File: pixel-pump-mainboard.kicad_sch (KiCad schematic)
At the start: 121 parts, among them J1 JST NC Valve, J10 BM10B-SRSS-TB(LF)(SN), J11 UART/SWD DNP, J12 TYPE-C-31-M-12, J2 JST NO Valve, J3 6P4C, J4 JST 3 Way Valve, J5 Jack-DC 12V, J6 Power Sw, J7 EXP1, J8 EXP2, J9 BM04B-SRSS-TBT(LF)(SN), Q1 BSS138, Q2 BSS138, Q3 BSS138, Q4 STN4NF20L, Q5 BSS138, SW1 BOOTSEL, U1 LD1117S33TR, U2 TPS62112RSAR, U3 W25Q128JVS, U4 RP2040, Y1 445C25D12M00000

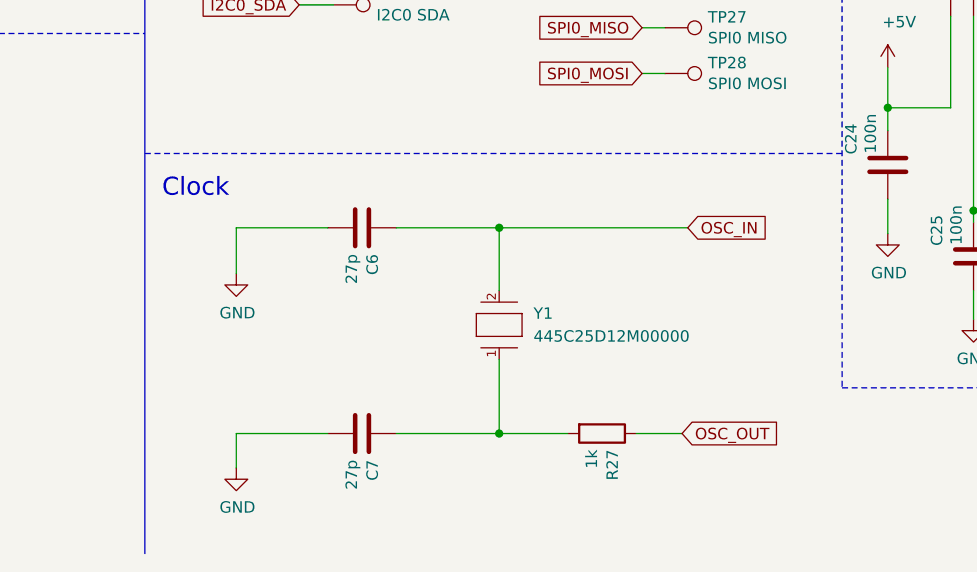
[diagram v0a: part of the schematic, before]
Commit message: Revert back to ABM12 footprint
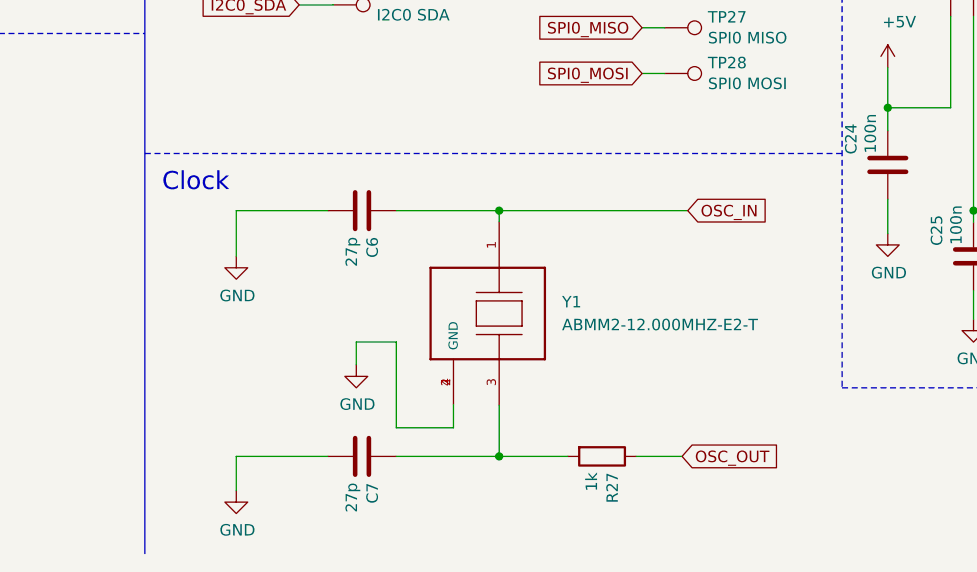
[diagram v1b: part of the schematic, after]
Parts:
- removed Y1: 445C25D12M00000, CTS 445C25D12M00000 12MHz:CTS-445-0-0-0, symbol CTS 445C25D12M00000 12MHz:445C25D12M00000
- added Y1: ABMM2-12.000MHZ-E2-T, ABMM2-12:XTAL_ABMM2-12.000MHZ-E2-T, symbol ABMM2-12.000MHZ-E2-T:ABMM2-12.000MHZ-E2-T
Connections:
- net GND: now also Y1.2 (GND), Y1.4 (GND)
- net OSC_IN: now also Y1.1
- net at C7.1, R27.2: now also Y1.3
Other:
- company: (none) -> Robins Tools
- moved on the sheet: C6, C7, R27

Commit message: Assign all MPNs
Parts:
- C1, C5: MPN (none) -> C3225X5R1E106K250AA
- C10, C12, C13, C16, C17, C18, C19, C20, C22, C23: MPN (none) -> 100n 0402
- C11: MPN (none) -> 10u 0603
- C14, C15: MPN (none) -> 2.2u 0402
- C2: MPN (none) -> 1u 0805
- C21: MPN (none) -> 1n 0603
- C24, C25, C26, C27, C3, C8: MPN (none) -> 100n 0603
- C28, C9, J11: MPN (none) -> DNP
- C4: value 22u 10V -> 22u 16V; MPN (none) -> C3225X7R1C226M250AC
- C6, C7: MPN (none) -> 27p 0603
- D1, D4, D6: MPN (none) -> SP0502BAHT
- D10, D3, D9: MPN (none) -> SOD4007
- D2, D7, D8: MPN (none) -> ORH-G36G DNP
- D5: MPN (none) -> SMAJ12CA
- F1: MPN (none) -> 1812L075PR
- J10: MPN (none) -> BM10B-SRSS-TB(LF)(SN)
- J12: MPN (none) -> TYPE-C-31-M-12
- J3: MPN (none) -> DS1133-S40BPX
- J5: MPN (none) -> 694106301002
- J6: MPN (none) -> WJ500V-5.08-2P; Source https://lcsc.com/product-detail/Pluggable-System-Terminal-B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 -> https://www.lcsc.com/product-detail/Screw-terminal_Ningbo-K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
- J7: MPN (none) -> BM04B-SRSS-TB(LF)(SN)
- J8: MPN (none) -> BM06B-SRSS-TB(LF)(SN)
- J9: MPN (none) -> BM04B-SRSS-TBT(LF)(SN)
- L1, L2: MPN (none) -> SLF7032T-6R8M1R6-2-PF
- Q1, Q2, Q3, Q5: MPN (none) -> BSS138
- Q4: MPN (none) -> STN4NF20L
- R1: MPN (none) -> 5.1k 0402
- R10, R12, R8: MPN (none) -> 68k 0603 DNP
- R11, R6, R9: MPN (none) -> 100k 0603
- R13: MPN (none) -> 100 0603
- R14, R3: MPN (none) -> 1M 0603
- R15, R17, R23, R24, R7: MPN (none) -> 220 0603
- R19: MPN (none) -> 0 0805 DNP
- R2: MPN (none) -> 5.1k 0603
- R20, R25, R29: MPN (none) -> 10k 0603
- R21, R22: MPN (none) -> 2.2k 0603
- R26, R27: MPN (none) -> 1k 0603
- R28: MPN (none) -> 10k 0603 DNP
- R4, R5: MPN (none) -> 27.4 0402
- SW1: MPN (none) -> 1825027-5
- U1: MPN (none) -> LD1117S33TR
- U3: value W25Q128JVS -> W25Q128JVPIQ; MPN (none) -> W25Q128JVPIQ
- U4: MPN (none) -> RP2040
- Y1: MPN (none) -> ABMM2-12.000MHZ-E2-T

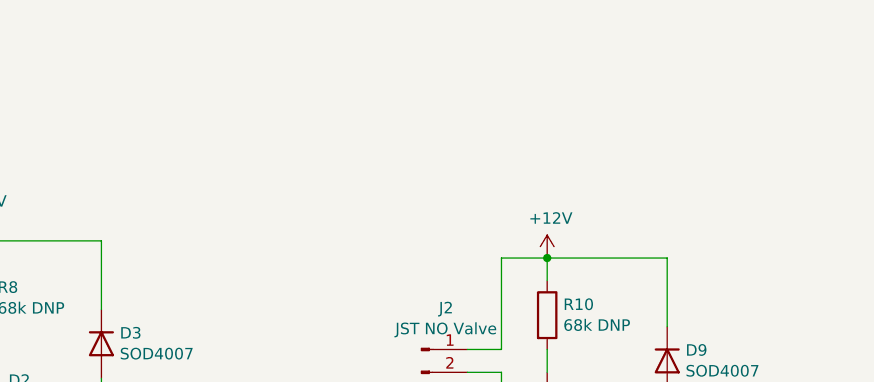
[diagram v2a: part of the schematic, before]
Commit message: Add fiducials and fix THT parts to be SMD
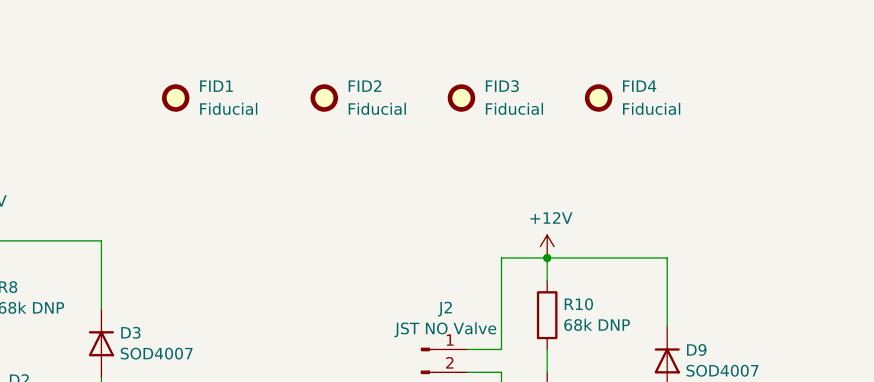
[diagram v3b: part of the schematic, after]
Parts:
- added FID1, FID2, FID3, FID4: Fiducial, Fiducial:Fiducial_0.5mm_Mask1mm, symbol Mechanical:Fiducial
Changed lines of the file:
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@@
+    )
+  )
+  (symbol (lib_id "Mechanical:Fiducial") (at 111.76 21.59 0) (unit 1)
+    (in_bom yes) (on_board yes) (fields_autoplaced)
+    (property "Reference" "FID3" (id 0) (at 114.3 20.3199 0)
+      (effects (font (size 1.27 1.27)) (justify left))
+    )
+    (property "Value" "Fiducial" (id 1) (at 114.3 22.8599 0)
+      (effects (font (size 1.27 1.27)) (justify left))
+    )
+    (property "Footprint" "Fiducial:Fiducial_0.5mm_Mask1mm" (id 2) (at 111.76 21.59 0)
+      (effects (font (size 1.27 1.27)) hide)
+    )
+    (property "Datasheet" "~" (id 3) (at 111.76 21.59 0)
+      (effects (font (size 1.27 1.27)) hide)
     )
   )
@@
     )
     (pin "1")
+  )
+  (symbol (lib_id "Mechanical:Fiducial") (at 80.01 21.59 0) (unit 1)
+    (in_bom yes) (on_board yes) (fields_autoplaced)
+    (property "Reference" "FID1" (id 0) (at 82.55 20.3199 0)
+      (effects (font (size 1.27 1.27)) (justify left))
+    )
+    (property "Value" "Fiducial" (id 1) (at 82.55 22.8599 0)
+      (effects (font (size 1.27 1.27)) (justify left))
+    )
+    (property "Footprint" "Fiducial:Fiducial_0.5mm_Mask1mm" (id 2) (at 80.01 21.59 0)
+      (effects (font (size 1.27 1.27)) hide)
+    )
+    (property "Datasheet" "~" (id 3) (at 80.01 21.59 0)
+      (effects (font (size 1.27 1.27)) hide)
+    )
   )
   (symbol (lib_id "Device:C") (at 199.39 132.08 0) (unit 1)
@@
     (pin "1")
   )
+  (symbol (lib_id "Mechanical:Fiducial") (at 127 21.59 0) (unit 1)
+    (in_bom yes) (on_board yes) (fields_autoplaced)
+    (property "Reference" "FID4" (id 0) (at 129.54 20.3199 0)
+      (effects (font (size 1.27 1.27)) (justify left))
+    )
+    (property "Value" "Fiducial" (id 1) (at 129.54 22.8599 0)
+      (effects (font (size 1.27 1.27)) (justify left))
+    )
+    (property "Footprint" "Fiducial:Fiducial_0.5mm_Mask1mm" (id 2) (at 127 21.59 0)
+      (effects (font (size 1.27 1.27)) hide)
+    )
+    (property "Datasheet" "~" (id 3) (at 127 21.59 0)
+      (effects (font (size 1.27 1.27)) hide)
+    )
+  )
   (symbol (lib_id "TYPE-C-31-M-12:TYPE-C-31-M-12") (at 57.15 235.585 0) (unit 1)
     (in_bom yes) (on_board yes)
@@
     )
   )
+  (symbol (lib_id "Mechanical:Fiducial") (at 96.52 21.59 0) (unit 1)
+    (in_bom yes) (on_board yes) (fields_autoplaced)
+    (property "Reference" "FID2" (id 0) (at 99.06 20.3199 0)
+      (effects (font (size 1.27 1.27)) (justify left))
+    )
+    (property "Value" "Fiducial" (id 1) (at 99.06 22.8599 0)
+      (effects (font (size 1.27 1.27)) (justify left))
+    )
+    (property "Footprint" "Fiducial:Fiducial_0.5mm_Mask1mm" (id 2) (at 96.52 21.59 0)
+      (effects (font (size 1.27 1.27)) hide)
+    )
+    (property "Datasheet" "~" (id 3) (at 96.52 21.59 0)
+      (effects (font (size 1.27 1.27)) hide)
+    )
+  )
   (sheet_instances
     (path "/" (page "1"))
@@
       (reference "F1") (unit 1) (value "1812L075PR") (footprint "Fuse:Fuse_1812_4532Metric")
     )
+    (path "/525bcaf8-d6f5-4066-bfb1-6ce2476103cc"
+      (reference "FID1") (unit 1) (value "Fiducial") (footprint "Fiducial:Fiducial_0.5mm_Mask1mm")
+    )
+    (path "/ff9e6f2a-ecb8-41c5-8eb1-61a3a0969262"
+      (reference "FID2") (unit 1) (value "Fiducial") (footprint "Fiducial:Fiducial_0.5mm_Mask1mm")
+    )
+    (path "/1b6bfdd4-98c5-406d-bac2-cc06853dcd37"
+      (reference "FID3") (unit 1) (value "Fiducial") (footprint "Fiducial:Fiducial_0.5mm_Mask1mm")
+    )
+    (path "/f50fdb03-4e54-439a-b508-d878f9afad01"
+      (reference "FID4") (unit 1) (value "Fiducial") (footprint "Fiducial:Fiducial_0.5mm_Mask1mm")
+    )
     (path "/3d163751-7871-486d-a542-8b4f1d680a2a"

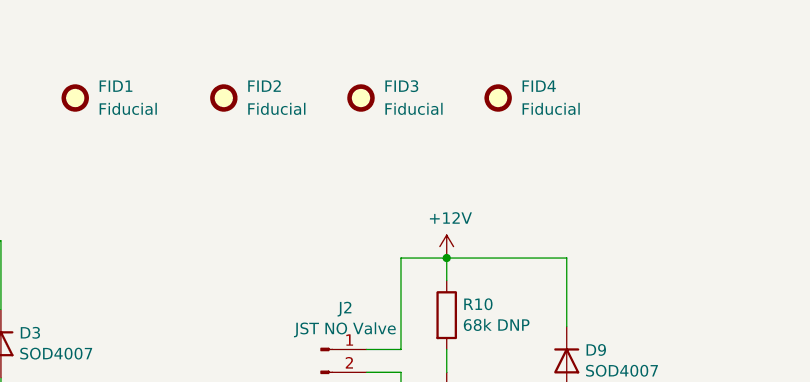
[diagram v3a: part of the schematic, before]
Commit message: Remove DNP parts from BOM, increase Fiducial to 0.75/1.5mm
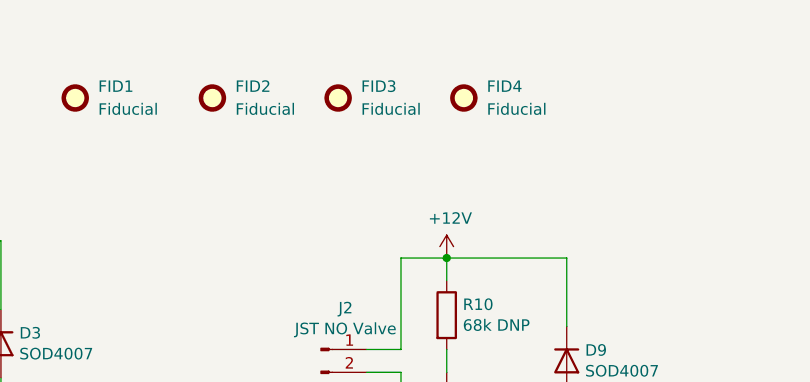
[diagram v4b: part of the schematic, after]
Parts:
- D2, R8: now left out of the parts list
- FID1, FID2, FID3, FID4: footprint Fiducial:Fiducial_0.5mm_Mask1mm -> Fiducial:Fiducial_0.75mm_Mask1.5mm
- J1, J2, J4: MPN (none) -> B2B-XH-A-GU
- Q1, Q2, Q3: MPN BSS138 -> BSS138P
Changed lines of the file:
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@@
       (effects (font (size 1.27 1.27)) (justify left) hide)
     )
-    (property "MPN" "BSS138" (id 4) (at 55.88 67.945 0)
+    (property "MPN" "BSS138P" (id 4) (at 55.88 67.945 0)
       (effects (font (size 1.27 1.27)) hide)
     )
@@
   )
   (symbol (lib_id "Device:R") (at 58.42 43.815 0) (unit 1)
-    (in_bom yes) (on_board yes)
+    (in_bom no) (on_board yes)
     (property "Reference" "R8" (id 0) (at 60.198 42.6466 0)
       (effects (font (size 1.27 1.27)) (justify left))
@@
   )
   (symbol (lib_id "Device:LED") (at 58.42 53.975 90) (unit 1)
-    (in_bom yes) (on_board yes)
+    (in_bom no) (on_board yes)
     (property "Reference" "D2" (id 0) (at 61.4172 52.9844 90)
       (effects (font (size 1.27 1.27)) (justify right))
@@
       (effects (font (size 1.27 1.27)) hide)
     )
+    (property "MPN" "B2B-XH-A-GU" (id 5) (at 44.45 47.625 0)
+      (effects (font (size 1.27 1.27)) hide)
+    )
     (pin "1")
     (pin "2")
@@
       (effects (font (size 1.27 1.27)) (justify left) hide)
     )
-    (property "MPN" "BSS138" (id 4) (at 118.745 69.85 0)
+    (property "MPN" "BSS138P" (id 4) (at 118.745 69.85 0)
       (effects (font (size 1.27 1.27)) hide)
     )
@@
       (effects (font (size 1.27 1.27)) hide)
     )
+    (property "MPN" "B2B-XH-A-GU" (id 5) (at 107.315 49.53 0)
+      (effects (font (size 1.27 1.27)) hide)
+    )
     (pin "1")
     (pin "2")
@@
       (effects (font (size 1.27 1.27)) (justify left) hide)
     )
-    (property "MPN" "BSS138" (id 4) (at 179.07 69.85 0)
+    (property "MPN" "BSS138P" (id 4) (at 179.07 69.85 0)
       (effects (font (size 1.27 1.27)) hide)
     )
@@
       (effects (font (size 1.27 1.27)) hide)
     )
+    (property "MPN" "B2B-XH-A-GU" (id 5) (at 167.64 49.53 0)
+      (effects (font (size 1.27 1.27)) hide)
+    )
     (pin "1")
     (pin "2")
@@
     )
   )
-  (symbol (lib_id "Mechanical:Fiducial") (at 111.76 21.59 0) (unit 1)
-    (in_bom yes) (on_board yes) (fields_autoplaced)
-    (property "Reference" "FID3" (id 0) (at 114.3 20.3199 0)
-      (effects (font (size 1.27 1.27)) (justify left))
-    )
-    (property "Value" "Fiducial" (id 1) (at 114.3 22.8599 0)
-      (effects (font (size 1.27 1.27)) (justify left))
-    )
-    (property "Footprint" "Fiducial:Fiducial_0.5mm_Mask1mm" (id 2) (at 111.76 21.59 0)
-      (effects (font (size 1.27 1.27)) hide)
-    )
-    (property "Datasheet" "~" (id 3) (at 111.76 21.59 0)
-      (effects (font (size 1.27 1.27)) hide)
-    )
-  )
   (symbol (lib_id "Mechanical:MountingHole") (at 233.045 20.955 0) (unit 1)
     (in_bom no) (on_board yes) (fields_autoplaced)
@@
       (effects (font (size 1.27 1.27)) (justify left))
     )
-    (property "Footprint" "Fiducial:Fiducial_0.5mm_Mask1mm" (id 2) (at 80.01 21.59 0)
+    (property "Footprint" "Fiducial:Fiducial_0.75mm_Mask1.5mm" (id 2) (at 80.01 21.59 0)
       (effects (font (size 1.27 1.27)) hide)
     )
@@
     (pin "1")
   )
+  (symbol (lib_id "Mechanical:Fiducial") (at 123.19 21.59 0) (unit 1)
+    (in_bom yes) (on_board yes) (fields_autoplaced)
+    (property "Reference" "FID4" (id 0) (at 125.73 20.3199 0)
+      (effects (font (size 1.27 1.27)) (justify left))
+    )
+    (property "Value" "Fiducial" (id 1) (at 125.73 22.8599 0)
+      (effects (font (size 1.27 1.27)) (justify left))
+    )
+    (property "Footprint" "Fiducial:Fiducial_0.75mm_Mask1.5mm" (id 2) (at 123.19 21.59 0)
+      (effects (font (size 1.27 1.27)) hide)
+    )
+    (property "Datasheet" "~" (id 3) (at 123.19 21.59 0)
+      (effects (font (size 1.27 1.27)) hide)
+    )
+  )
   (symbol (lib_id "power:GND") (at 329.565 156.21 0) (unit 1)
     (in_bom yes) (on_board yes)
@@
     (pin "2")
   )
+  (symbol (lib_id "Mechanical:Fiducial") (at 109.22 21.59 0) (unit 1)
+    (in_bom yes) (on_board yes) (fields_autoplaced)
+    (property "Reference" "FID3" (id 0) (at 111.76 20.3199 0)
+      (effects (font (size 1.27 1.27)) (justify left))
+    )
+    (property "Value" "Fiducial" (id 1) (at 111.76 22.8599 0)
+      (effects (font (size 1.27 1.27)) (justify left))
+    )
+    (property "Footprint" "Fiducial:Fiducial_0.75mm_Mask1.5mm" (id 2) (at 109.22 21.59 0)
+      (effects (font (size 1.27 1.27)) hide)
+    )
+    (property "Datasheet" "~" (id 3) (at 109.22 21.59 0)
+      (effects (font (size 1.27 1.27)) hide)
+    )
+  )
   (symbol (lib_id "Device:C") (at 325.755 33.02 0) (unit 1)
     (in_bom yes) (on_board yes)
@@
     (pin "2")
   )
+  (symbol (lib_id "Mechanical:Fiducial") (at 95.25 21.59 0) (unit 1)
+    (in_bom yes) (on_board yes) (fields_autoplaced)
+    (property "Reference" "FID2" (id 0) (at 97.79 20.3199 0)
+      (effects (font (size 1.27 1.27)) (justify left))
+    )
+    (property "Value" "Fiducial" (id 1) (at 97.79 22.8599 0)
+      (effects (font (size 1.27 1.27)) (justify left))
+    )
+    (property "Footprint" "Fiducial:Fiducial_0.75mm_Mask1.5mm" (id 2) (at 95.25 21.59 0)
+      (effects (font (size 1.27 1.27)) hide)
+    )
+    (property "Datasheet" "~" (id 3) (at 95.25 21.59 0)
+      (effects (font (size 1.27 1.27)) hide)
+    )
+  )
   (symbol (lib_id "Device:C") (at 362.585 36.195 180) (unit 1)
     (in_bom yes) (on_board yes)
@@
     (pin "1")
   )
-  (symbol (lib_id "Mechanical:Fiducial") (at 127 21.59 0) (unit 1)
-    (in_bom yes) (on_board yes) (fields_autoplaced)
-    (property "Reference" "FID4" (id 0) (at 129.54 20.3199 0)
-      (effects (font (size 1.27 1.27)) (justify left))
-    )
-    (property "Value" "Fiducial" (id 1) (at 129.54 22.8599 0)
-      (effects (font (size 1.27 1.27)) (justify left))
-    )
-    (property "Footprint" "Fiducial:Fiducial_0.5mm_Mask1mm" (id 2) (at 127 21.59 0)
-      (effects (font (size 1.27 1.27)) hide)
-    )
-    (property "Datasheet" "~" (id 3) (at 127 21.59 0)
-      (effects (font (size 1.27 1.27)) hide)
-    )
-  )
   (symbol (lib_id "TYPE-C-31-M-12:TYPE-C-31-M-12") (at 57.15 235.585 0) (unit 1)
     (in_bom yes) (on_board yes)
@@
     )
   )
-  (symbol (lib_id "Mechanical:Fiducial") (at 96.52 21.59 0) (unit 1)
-    (in_bom yes) (on_board yes) (fields_autoplaced)
-    (property "Reference" "FID2" (id 0) (at 99.06 20.3199 0)
-      (effects (font (size 1.27 1.27)) (justify left))
-    )
-    (property "Value" "Fiducial" (id 1) (at 99.06 22.8599 0)
-      (effects (font (size 1.27 1.27)) (justify left))
-    )
-    (property "Footprint" "Fiducial:Fiducial_0.5mm_Mask1mm" (id 2) (at 96.52 21.59 0)
-      (effects (font (size 1.27 1.27)) hide)
-    )
-    (property "Datasheet" "~" (id 3) (at 96.52 21.59 0)
-      (effects (font (size 1.27 1.27)) hide)
-    )
-  )
   (sheet_instances
     (path "/" (page "1"))
@@
     )
     (path "/525bcaf8-d6f5-4066-bfb1-6ce2476103cc"
-      (reference "FID1") (unit 1) (value "Fiducial") (footprint "Fiducial:Fiducial_0.5mm_Mask1mm")
+      (reference "FID1") (unit 1) (value "Fiducial") (footprint "Fiducial:Fiducial_0.75mm_Mask1.5mm")
     )
-    (path "/ff9e6f2a-ecb8-41c5-8eb1-61a3a0969262"
-      (reference "FID2") (unit 1) (value "Fiducial") (footprint "Fiducial:Fiducial_0.5mm_Mask1mm")
+    (path "/e1c5bd5e-ecc6-4829-9336-9b05cc6a9ba6"
+      (reference "FID2") (unit 1) (value "Fiducial") (footprint "Fiducial:Fiducial_0.75mm_Mask1.5mm")
     )
-    (path "/1b6bfdd4-98c5-406d-bac2-cc06853dcd37"
-      (reference "FID3") (unit 1) (value "Fiducial") (footprint "Fiducial:Fiducial_0.5mm_Mask1mm")
+    (path "/ce5e1b2e-d22e-4c1d-81e4-f4519c1dd12f"
+      (reference "FID3") (unit 1) (value "Fiducial") (footprint "Fiducial:Fiducial_0.75mm_Mask1.5mm")
     )
-    (path "/f50fdb03-4e54-439a-b508-d878f9afad01"
-      (reference "FID4") (unit 1) (value "Fiducial") (footprint "Fiducial:Fiducial_0.5mm_Mask1mm")
+    (path "/571984ba-bd34-432e-b8b7-0b15b354dfb5"
+      (reference "FID4") (unit 1) (value "Fiducial") (footprint "Fiducial:Fiducial_0.75mm_Mask1.5mm")
     )
     (path "/3d163751-7871-486d-a542-8b4f1d680a2a"
